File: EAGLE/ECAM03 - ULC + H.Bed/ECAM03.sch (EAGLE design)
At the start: 50 parts, among them J1 MODULAR TOOL, J2 SPI, J3 MOT, J4 FTDI, J5 S4B-PH-SM4, J6 S5B-PH-SM, J7 RINGLIGHT, Q2 16MHz, U1 SP3485, U2 ATMEGA238, U3 DRV8825, U4 NTR4003NT3G, U5 NTR4003NT3G, U6 NTR4003NT3G, U7 NTR4003NT3G, U8 AP3032, X1 MPXV5100DP

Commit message: Created preliminary final schematic for ECA03
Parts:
- removed C1, C10: 10nF, TinWhiskers:CPL-CAP-X7R-0603-10NF-50V
- removed C11: 470pF, TinWhiskers:CPL-CAP-X7R-0603-470PF-100V
- removed C2: 100nF, TinWhiskers:CPL-CAP-X7R-0603-100NF-50V
- removed C3, C7, C8, C9: 1uF, TinWhiskers:CPL-CAP-X5R-0603-1UF-50V
- removed C6: 0.1uF, TinWhiskers:CPL-CAP-X7R-0603-100NF-50V
- removed J6: S5B-PH-SM, TinWhiskers:CPL-CON-JST-2.0MM-5P-M-SMT-RA
- removed R12, R14: 10K, TinWhiskers:CPL-RES-0603-10K-0.1W
- removed R6: 0R22, TinWhiskers:CPL-RES-1206-0.22-0.5W
- removed R7: 20K, TinWhiskers:CPL-RES-0603-20K-0.1W
- removed U6: NTR4003NT3G, TinWhiskers:CPL-MOSFET-NCH-SOT23
- removed VR1: TC1015-3.3VCT713, TinWhiskers:CPL-REG-LIN-3.3V-0.1A
- removed X1: MPXV5100DP, TinWhiskers:CPL-SEN-PRS-MPXV5100DP
- J2: value SPI -> FAN1; device TinWhiskers:CPL-CON-HEADER-0.1IN-6P-M -> TinWhiskers:CPL-CON-HEADER-0.1IN-3P-M; PARTNO 67996-206HLF -> (none)
- J3: value MOT -> FAN2; device TinWhiskers:CPL-CON-JST-2.0MM-4P-M-RA -> TinWhiskers:CPL-CON-HEADER-0.1IN-3P-M; PARTNO S4B-PH-SM4-TB(LF)(SN) -> (none)
- J4: value FTDI -> FAN3; device TinWhiskers:CPL-CON-JST-2.0MM-6P-M-RA -> TinWhiskers:CPL-CON-HEADER-0.1IN-3P-M; PARTNO S6B-PH-SM4-TB(LF)(SN) -> (none)
- R1: device TinWhiskers:TC33X-2 -> TinWhiskers:CPL-RES-0603-10K-0.1W; PARTNO TC33X-2-103E -> (none)
- R5: value 0R22 -> 5K; device TinWhiskers:CPL-RES-1206-0.22-0.5W -> TinWhiskers:CPL-RES-0603-5K-0.1W; PARTNO RL1206FR-7W0R22L -> (none)
- U3: value DRV8825 -> MCP4725; device TinWhiskers:CPL-MDR-DRV8825 -> TinWhiskers:CPL-DAC-12BIT-SOT23; PARTNO DRV8825PWPR -> (none)
- U4: value NTR4003NT3G -> MAX31855; device TinWhiskers:CPL-MOSFET-NCH-SOT23 -> TinWhiskers:CPL-THRM-MAX31855
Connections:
- removed net !ENBL: U2.PD5, U3.!ENBL
- removed net AOUT1: J3.1, U3.AOUT1
- removed net AOUT2: J3.2, U3.AOUT2
- removed net BOUT1: J3.3, U3.BOUT1
- removed net BOUT2: J3.4, U3.BOUT2
- removed net DIR: U3.DIR
- removed net GATE1: U2.PC1, U4.GATE
- removed net GATE2: U2.PC2, U5.GATE
- removed net GATE3: U2.PC3, U6.GATE
- removed net GATE4: U2.PC4, U7.GATE
- removed net N$13: C3.2, R7.1, U3.MODE0, U3.MODE1, U3.MODE2, U3.V3P3OUT
- removed net N$14: R1.E, R7.2
- removed net N$15: R1.S, U3.AVREF, U3.BVREF
- removed net N$16: C6.1, J4.6
- removed net N$6: C1.1, U3.CP2
- removed net N$7: C2.2, U3.VCP
- removed net N$8: R5.2, U3.ISENA
- removed net N$9: R6.2, U3.ISENB
- removed net SOL1: J6.2, U4.DRAIN
- removed net SOL2: J6.3, U5.DRAIN
- removed net SOL3: J6.4, U6.DRAIN
- removed net SOL4: J6.5, U7.DRAIN
- removed net STEP: U2.PD3, U3.STEP
- new net A0: U3.A0
- new net CPWR: J5.4, U7.DRAIN
- new net FAN: U2.PD5, U5.GATE
- new net FPWR: J2.2, J3.2, J4.2, U5.DRAIN
- new net SCL: U2.PC5, U3.SCL
- new net SDA: U2.PC4, U3.SDA
- new net SSR: U2.PD3
- new net T+: U4.T+
- new net T-: U4.T-
- new net TACH1: J2.3, U2.PC1
- new net TACH2: J3.3, U2.PC2
- new net TACH3: J4.3, U2.PC3
- net +24V: now also J2.1, J3.1, J4.1; no longer C2.1, U3.VMA, U3.VMB
- net +3V3: no longer C8.2, VR1.5
- net +5V: now also R1.1, U3.VDD, U4.VCC, U7.GATE; no longer C10.2, C7.2, C9.2, J2.2, J4.3, J5.4, J6.1, R12.2, R14.1, U3.!RESET, U3.!SLEEP, VR1.1, VR1.3, X1.VS
- net DI: no longer J4.5
- net GND: now also U3.VSS, U4.GND; no longer C10.1, C11.1, C3.1, C7.1, C8.1, C9.1, J2.6, J4.1, J4.2, R1.A, R6.1, U3.GND@14, U3.GND@28, U3.PAD, U4.SOURCE, U6.SOURCE, X1.GND
- net MISO: now also U4.SO; no longer J2.1
- net MOSI: no longer J2.4
- net N$5: now also R5.2, U3.VOUT; no longer C1.2, U3.CP1
- net RESET: no longer C6.2, J2.5, R12.1
- net RO: no longer J4.4
- net SCK: now also U4.SCK; no longer J2.3
- net SS: now also R1.2, U4.!CS; no longer R14.2
- net VOUT: no longer C11.2, X1.VOUT
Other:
- note added: "DAC"
- note added: "ECAM03 - Up-Looking Camera & Heated Bed Control"
- note added: "FAN CONNEX"
- note added: "FAN SWITCH"
- note added: "THERM"
- note added: "USB PWR"
- note removed: "End Effector Control and USB Passthrough"
- note removed: "FTDI INTERFACE"
- note removed: "PRESSURE TRANSDUCER"
- note removed: "SOLENOIDS"
- note removed: "SPI INTERFACE"
- note removed: "STEPPER MTR DRIVER"
- note removed: "V-REG (5V-3.3V)"
- moved on the sheet: C12, C4, C5, D1, J5, J7, L1, Q2, R10, R11, R13, R15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

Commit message: Component placement begun
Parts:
- added TB1: T-BLOCK, TinWhiskers:CPL-TBLK-SCR-2CKT-5.0MM
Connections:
- removed net O_OUT: U2.PD2
- net T+: now also TB1.2
- net T-: now also TB1.1
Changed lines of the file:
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@@
 <part name="P+9" library="supply1" deviceset="+24V" device=""/>
 <part name="P+11" library="supply1" deviceset="+24V" device=""/>
+<part name="TB1" library="TinWhiskers" deviceset="CPL-TBLK-SCR-2CKT-5.0MM" device="" value="T-BLOCK"/>
 </parts>
 <sheets>
@@
 <text x="15.24" y="241.3" size="6.35" layer="94" ratio="10">USB PASS-THRU</text>
 <text x="20.32" y="198.12" size="1.27" layer="94" ratio="12">* ONLY POPULATE RESISTORS NECESSARY TO SELECT CORRECT ROUTING</text>
-<text x="30.48" y="160.02" size="6.35" layer="94" ratio="10">USB PWR</text>
-<text x="114.3" y="160.02" size="6.35" layer="94" ratio="10">DAC</text>
-<text x="167.64" y="160.02" size="6.35" layer="94" ratio="10">THERM</text>
+<text x="30.48" y="162.56" size="6.35" layer="94" ratio="10">USB PWR</text>
+<text x="114.3" y="162.56" size="6.35" layer="94" ratio="10">DAC</text>
+<text x="167.64" y="162.56" size="6.35" layer="94" ratio="10">THERM</text>
 <text x="226.06" y="162.56" size="6.35" layer="94" ratio="10">FAN CONNEX</text>
 <text x="22.86" y="116.84" size="6.35" layer="94" ratio="10">FAN SWITCH</text>
@@
 <instance part="P+11" gate="1" x="276.86" y="157.48" smashed="yes">
 <attribute name="VALUE" x="273.558" y="158.496" size="1.778" layer="96"/>
+</instance>
+<instance part="TB1" gate="G$1" x="160.02" y="149.86" smashed="yes" rot="MR0">
+<attribute name="NAME" x="157.48" y="154.94" size="1.778" layer="95" font="vector" ratio="12"/>
+<attribute name="VALUE" x="157.48" y="152.908" size="1.27" layer="96" font="vector" ratio="10"/>
 </instance>
 </instances>
@@
 </segment>
 </net>
-<net name="O_OUT" class="0">
-<segment>
-<pinref part="U2" gate="G$1" pin="PD2"/>
-<wire x1="345.44" y1="226.06" x2="353.06" y2="226.06" width="0.1524" layer="91"/>
-<label x="347.98" y="226.06" size="1.778" layer="95" ratio="12"/>
-</segment>
-</net>
 <net name="VOUT" class="0">
 <segment>
@@
 <wire x1="172.72" y1="149.86" x2="165.1" y2="149.86" width="0.1524" layer="91"/>
 <label x="165.1" y="149.86" size="1.778" layer="95"/>
+<pinref part="TB1" gate="G$1" pin="1"/>
 </segment>
 </net>
@@
 <wire x1="172.72" y1="147.32" x2="165.1" y2="147.32" width="0.1524" layer="91"/>
 <label x="165.1" y="147.32" size="1.778" layer="95"/>
-</segment>
-</net>
+<pinref part="TB1" gate="G$1" pin="2"/>
+</segment>
+</net>

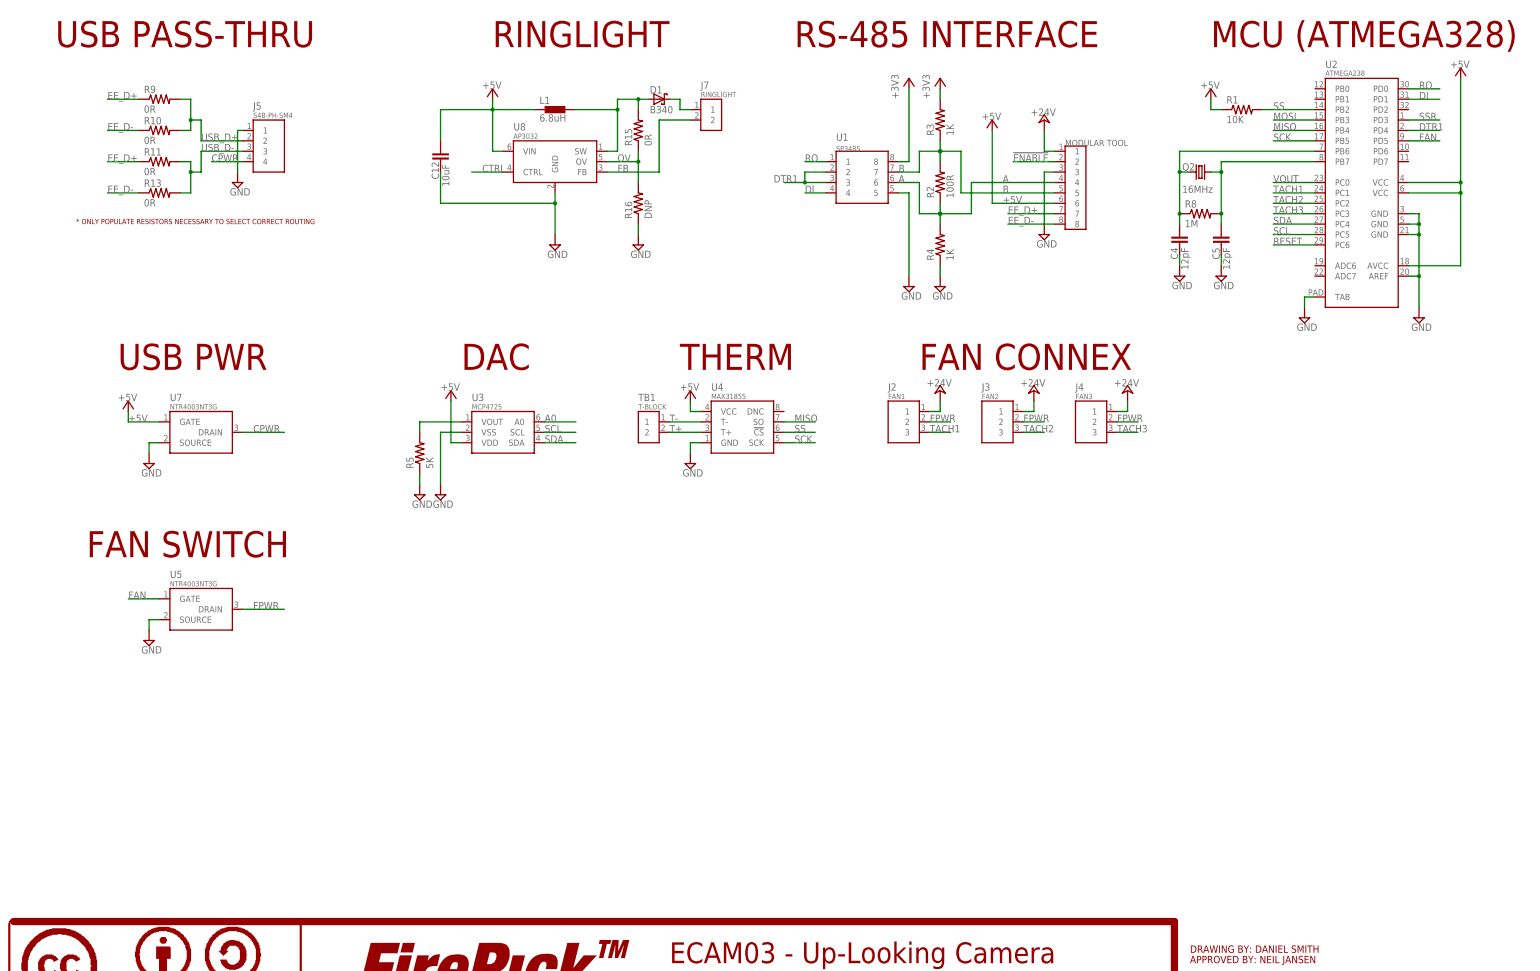
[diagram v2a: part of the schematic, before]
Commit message: Finalized schematics (minus potential LDO regulator) for all boards. Layout partially done for EFD01
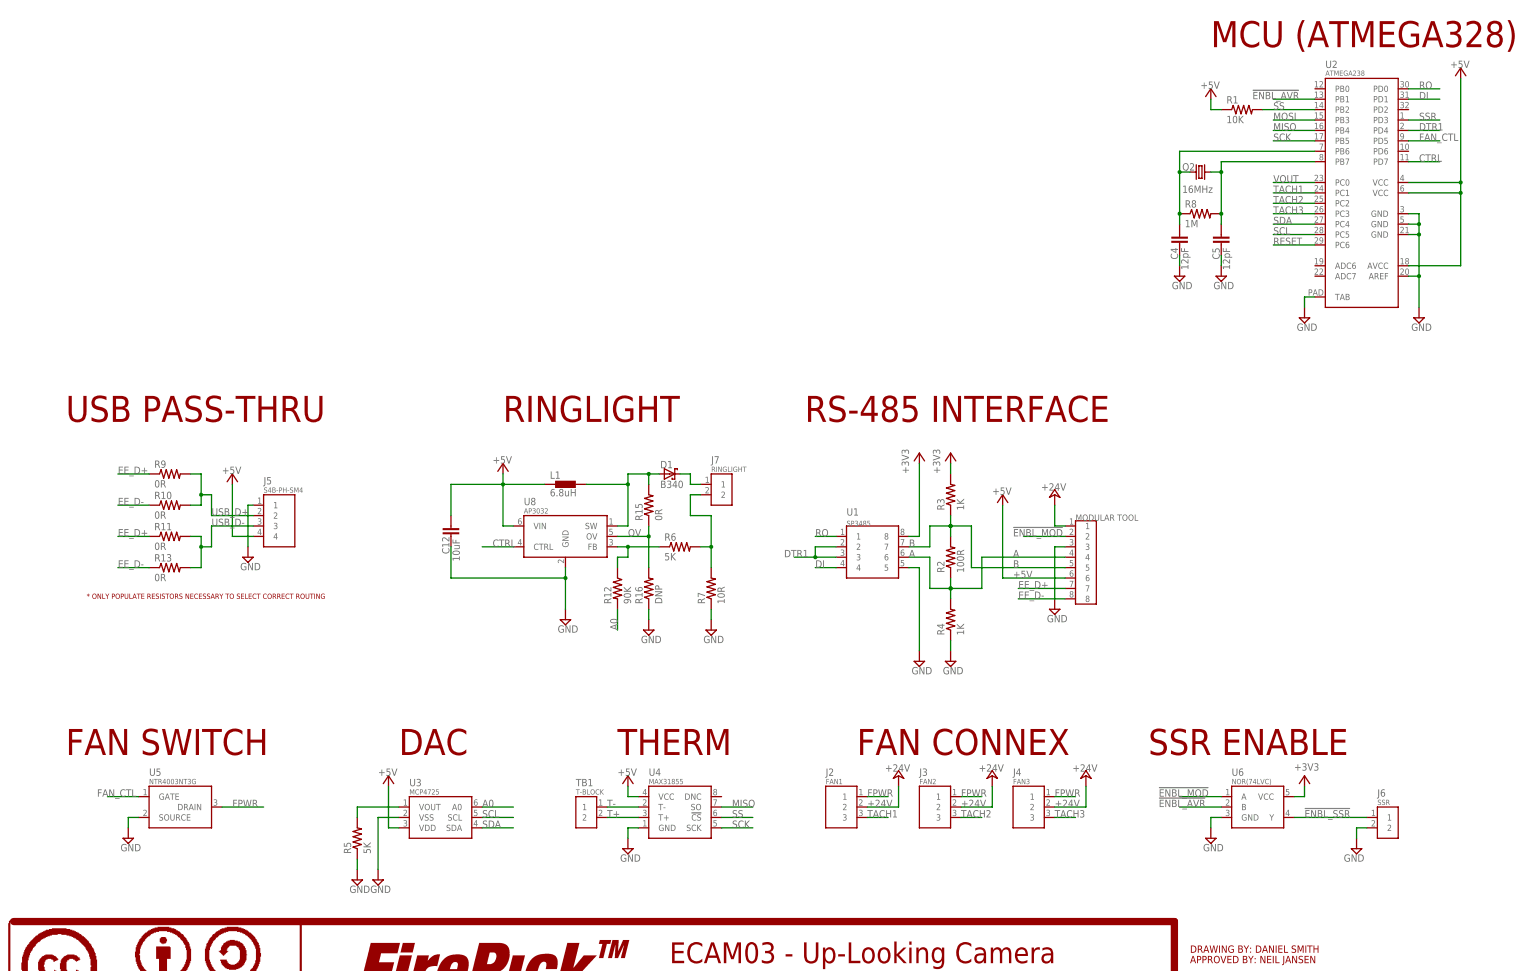
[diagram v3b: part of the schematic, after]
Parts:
- removed U7: NTR4003NT3G, TinWhiskers:CPL-MOSFET-NCH-SOT23
- added J6: SSR, TinWhiskers:CPL-CON-HEADER-0.1IN-2P-M
- added R12: 90K, TinWhiskers:CPL-RES-0603-90K-0.1W
- added R6: 5K, TinWhiskers:CPL-RES-0603-5K-0.1W
- added R7: 10R, TinWhiskers:CPL-RES-0603-10.0-0.1W
- added U6: NOR(74LVC), TinWhiskers:CPL-IC-LOGIC-NOR-1CH-74LVC
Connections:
- net FAN renamed FAN_CTL
- removed net !ENABLE: J1.2
- removed net CPWR: J5.4, U7.DRAIN
- removed net FB: J7.2, U8.FB
- new net !ENBL_AVR: U2.PB1, U6.B
- new net !ENBL_MOD: J1.2, U6.A
- new net !ENBL_SSR: J6.1, U6.Y
- new net N$3: J7.2, R6.2, R7.2
- new net N$4: R12.1, R6.1, U8.FB
- net +24V: now also J2.2, J3.2, J4.2; no longer J2.1, J3.1, J4.1
- net +3V3: now also U6.VCC
- net +5V: now also J5.4; no longer U7.GATE
- net A0: now also R12.2
- net CTRL: now also U2.PD7
- net FPWR: now also J2.1, J3.1, J4.1; no longer J2.2, J3.2, J4.2
- net GND: now also J6.2, R7.1, U6.GND; no longer U7.SOURCE
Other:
- note added: "SSR ENABLE"
- note removed: "USB PWR"
- moved on the sheet: C12, D1, J2, J3, J4, J5, J7, L1, R10, R11, R13, R15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
